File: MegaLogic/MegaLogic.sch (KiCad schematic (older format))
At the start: 17 parts

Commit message: I accidentally solved the Even/Odd problem
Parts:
- added Q? (x4): BC557, Package_TO_SOT_THT:TO-92_Inline, symbol Transistor_BJT:BC557
- added Q? (x4): BC547, Package_TO_SOT_THT:TO-92_Inline, symbol Transistor_BJT:BC547
- added U? (x5): 4070, symbol 4xxx:4070
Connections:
- net Input1: now also U?.1, Q?.2 (B), Q?.2 (B), Q?.2 (B)
- net Input2: now also U?.2, Q?.2 (B), Q?.2 (B)
- net Input3: now also U?.5, Q?.2 (B)
- net Input4: now also U?.6
- net Input5: now also U?.1
- net Input6: now also U?.2
- net Input7: now also U?.5
- net Input8: now also U?.6
- net V+: now also Q?.1 (C), Q?.1 (C), Q?.1 (C), Q?.3 (E)
- net at U?.3: now also U?.9
- net at U?.4: now also U?.8
- net at U?.10: now also U?.13
- net Odd: now reaches U?.11
- net Odd: now also Q?.2 (B)
- net at U?.12: now also U?.10
- new net: Q?.1 (C), Q?.3 (E), Q?.3 (E)
- new net: Q?.3 (E), Q?.3 (E)
- new net: U?.3, U?.9
- new net: U?.4, U?.8
- new net Count1: Q?.1 (C), Q?.3 (E)
- new net Count2: Q?.3 (E)
- new net Even: Q?.1 (C)
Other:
- moved on the sheet: Q?, U?A, U?B, U?C, U?D, U?E

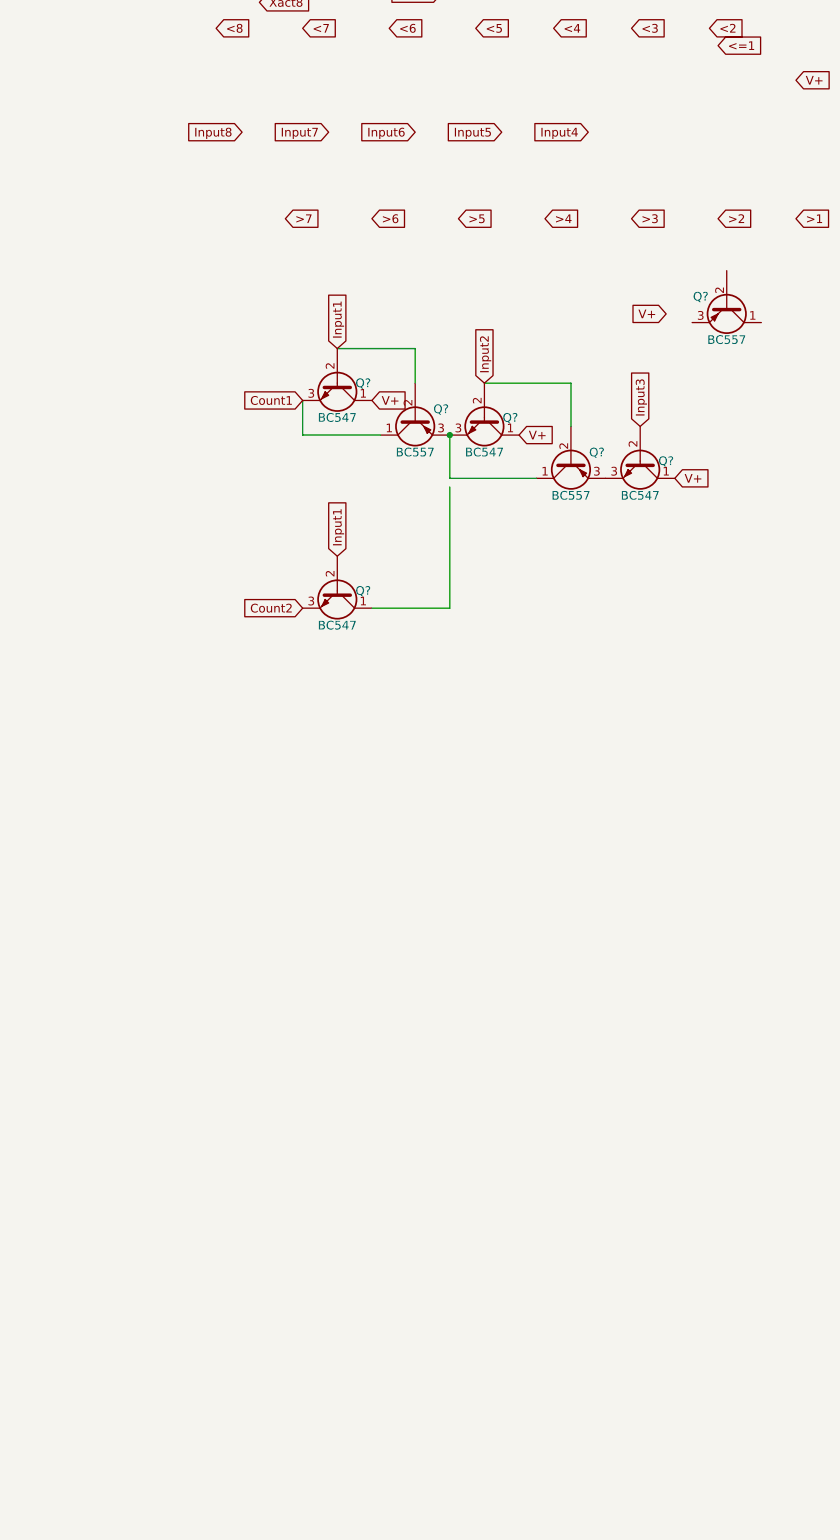
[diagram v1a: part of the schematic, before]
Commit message: I think I solved the Exact count problem
It is the same as the input sorting problem, could be combined?
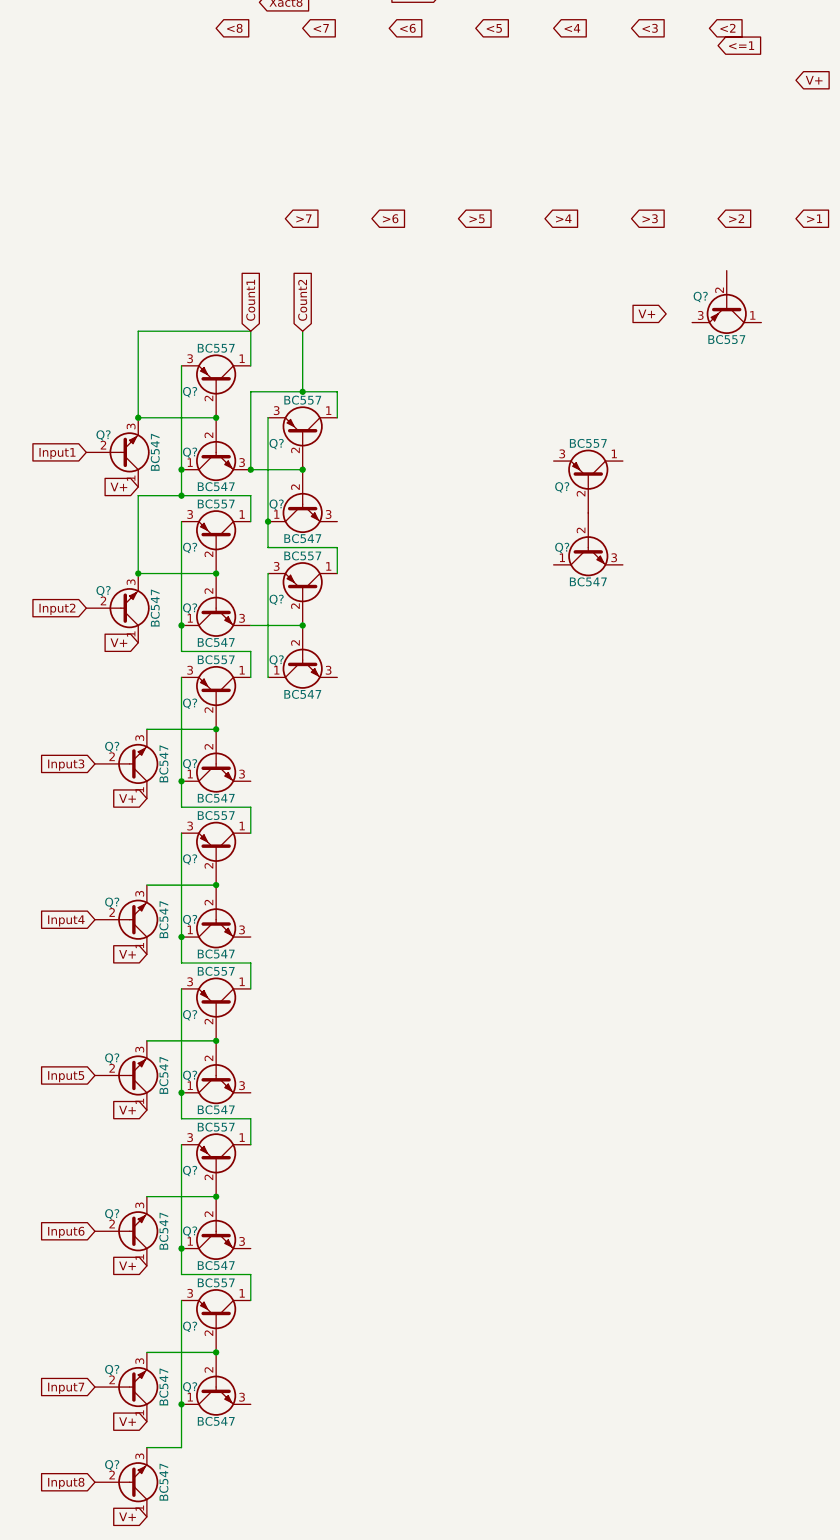
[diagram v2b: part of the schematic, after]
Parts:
- removed Q? (x3): BC547, Package_TO_SOT_THT:TO-92_Inline, symbol Transistor_BJT:BC547
- removed Q?: BC557, Package_TO_SOT_THT:TO-92_Inline, symbol Transistor_BJT:BC557
- added Q? (x17): BC547, Package_TO_SOT_THT:TO-92_Inline, symbol Transistor_BJT:BC547
- added Q? (x9): BC557, Package_TO_SOT_THT:TO-92_Inline, symbol Transistor_BJT:BC557
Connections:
- net Count1: now also Q?.2 (B), Q?.2 (B), Q?.3 (E); no longer Q?.3 (E)
- net Count2: now also Q?.3 (E), Q?.1 (C), Q?.2 (B), Q?.2 (B)
- net Input1: now also Q?.2 (B); no longer Q?.2 (B), Q?.2 (B)
- net Input2: now also Q?.2 (B)
- net Input3: now also Q?.2 (B)
- net Input4: now also Q?.2 (B)
- net Input5: now also Q?.2 (B)
- net Input6: now also Q?.2 (B)
- net Input7: now also Q?.2 (B)
- net Input8: now also Q?.2 (B)
- net V+: now also Q?.1 (C), Q?.1 (C), Q?.1 (C), Q?.1 (C), Q?.1 (C), Q?.1 (C), Q?.1 (C), Q?.1 (C); no longer Q?.1 (C)
- net at Q?.3 (E): now also Q?.1 (C), Q?.1 (C), Q?.2 (B), Q?.2 (B), Q?.3 (E)
- new net: Q?.2 (B), Q?.2 (B), Q?.3 (E) (x6)
- new net: Q?.1 (C), Q?.3 (E), Q?.3 (E)
- new net: Q?.1 (C), Q?.1 (C), Q?.3 (E) (x6)
- new net: Q?.2 (B), Q?.2 (B)
- new net: Q?.1 (C), Q?.3 (E)
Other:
- moved on the sheet: Q?

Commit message: Added Exactly and <> functions
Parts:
- removed Q? (x2): BC557, Package_TO_SOT_THT:TO-92_Inline, symbol Transistor_BJT:BC557
- removed Q?: BC547, Package_TO_SOT_THT:TO-92_Inline, symbol Transistor_BJT:BC547
- added Q? (x48): BC557, Package_TO_SOT_THT:TO-92_Inline, symbol Transistor_BJT:BC557
- added Q? (x55): BC547, Package_TO_SOT_THT:TO-92_Inline, symbol Transistor_BJT:BC547
- added U? (x10): 4069, symbol 4xxx:4070
- added U? (x7): 4069, symbol 4xxx:4069
- U? (x12): value 4070 -> 4069
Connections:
- net <2: now also U?.4
- net <3: now also U?.6
- net <4: now also U?.8
- net <5: now also U?.10
- net <6: now also U?.12
- net <7: now also U?.2
- net <8: now also Q?.1 (C)
- net InputJack1: now also Q?.2 (B)
- net InputJack2: now also Q?.2 (B)
- net InputJack3: now also Q?.2 (B)
- net InputJack4: now also Q?.2 (B)
- net InputJack6: now also Q?.2 (B)
- net InputJack7: now also Q?.2 (B)
- net InputJack8: now also Q?.2 (B)
- net V+: now also Q?.1 (C), Q?.1 (C), Q?.1 (C), Q?.1 (C), Q?.1 (C), Q?.1 (C), Q?.1 (C), Q?.1 (C), Q?.3 (E)
- net Xact1: now also U?.3
- net Xact2: now also U?.4
- net Xact3: now also U?.10
- net Xact4: now also U?.11
- net Xact5: now also U?.3
- net Xact6: now also U?.4
- net Xact7: now also U?.10
- net Xact8: now also Q?.2 (B), Q?.3 (E), U?.9
- net at Q?.2 (B), Q?.2 (B), Q?.3 (E): now also Q?.1 (C), Q?.1 (C), Q?.3 (E)
- net at Q?.3 (E): now also Q?.1 (C), Q?.3 (E), Q?.1 (C), Q?.2 (B), Q?.2 (B)
- net >=3: now reaches Q?.3 (E)
- net >=3: now also Q?.1 (C), Q?.2 (B), Q?.2 (B), U?.5, U?.5, U?.8
- net at Q?.3 (E): now also Q?.1 (C), Q?.1 (C), Q?.2 (B), Q?.2 (B), Q?.3 (E) (x4)
- net at Q?.3 (E): now also Q?.1 (C), Q?.3 (E)
- net Count1 renamed >=1
- net >=1: now also U?.2
- net Count2 renamed >=2
- net >=2: now also U?.1, U?.3, U?.6
- new net: Q?.1 (C), Q?.1 (C), Q?.2 (B), Q?.2 (B), Q?.3 (E), Q?.3 (E) (x25)
- new net: Q?.1 (C), Q?.3 (E), Q?.3 (E) (x12)
- new net: Q?.1 (C), Q?.2 (B), Q?.2 (B), Q?.3 (E) (x7)
- new net: Q?.2 (B), Q?.2 (B), Q?.3 (E) (x5)
- new net: Q?.1 (C), Q?.1 (C), Q?.3 (E) (x5)
- new net >=4: Q?.1 (C), Q?.2 (B), Q?.2 (B), Q?.3 (E), U?.12, U?.9, U?.9
- new net >=5: Q?.1 (C), Q?.2 (B), Q?.2 (B), Q?.3 (E), U?.11, U?.13, U?.2
- new net >=6: Q?.1 (C), Q?.2 (B), Q?.2 (B), Q?.3 (E), U?.1, U?.13, U?.5
- new net >=7: Q?.1 (C), Q?.2 (B), Q?.2 (B), Q?.3 (E), U?.1, U?.6, U?.8
- new net InputJack5: Q?.2 (B)
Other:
- note added: "<2-8"
- note added: "A1"
- note added: "A2"
- note added: "A3"
- note added: "A4"
- note added: "A5"
- note added: "A6"
- note added: "A7"
- note added: "B1"
- note added: "B2"
- note added: "B3"
- note added: "B4"
- note added: "B5"
- note added: "B6"
- note added: "C1"
- note added: "C2"
- note added: "C3"
- note added: "C4"
- note added: "C5"
- note added: "D1"
- note added: "D2"
- note added: "D3"
- note added: "D4"
- note added: "E1"
- note added: "E2"
- note added: "E3"
- note added: "F1"
- note added: "F2"
- note added: "G1"
- note removed: "<=2-8"
- moved on the sheet: Q?

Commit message: Added some new ideas
Problem with 3 voice synth library
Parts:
- added D?: LED, symbol Device:LED
- added D? (x3): D, symbol Device:D
- added J?: AudioJack2_SwitchT, symbol Connector:AudioJack2_SwitchT
- added Q?: BC547, Package_TO_SOT_THT:TO-92_Inline, symbol Transistor_BJT:BC547
- added R?: 15k, symbol Device:R
- added R? (x2): 1.2k, symbol Device:R
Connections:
- net >=1: now also D?.1 (K), Q?.2 (B), R?.2; no longer Q?.2 (B), Q?.2 (B), Q?.3 (E)
- net >=2: now also D?.1 (K); no longer Q?.2 (B), Q?.2 (B), Q?.3 (E)
- net >=3: now also D?.1 (K); no longer Q?.2 (B), Q?.2 (B), Q?.3 (E)
- net GND: now also D?.1 (K), J?.S
- net V+: now also Q?.1 (C)
- new net: D?.2 (A), Q?.2 (B), Q?.2 (B), Q?.3 (E) (x3)
- new net: J?.T, R?.1
- new net: D?.2 (A), R?.1
- new net: Q?.3 (E), R?.1, R?.2, R?.2
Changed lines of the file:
@@
 $EndComp
-Wire Wire Line
-	13000 750  13000 1200
 Wire Wire Line
 	13500 900  13500 750
@@
 Wire Wire Line
 	13000 1200 13300 1200
-Connection ~ 13000 1200
 Connection ~ 13300 1200
 Text Notes 12750 1250 0    50   ~ 10
@@
 	13000 600  13000 450
 Wire Wire Line
-	12350 900  12350 450
-Wire Wire Line
 	12350 450  13000 450
-Connection ~ 12350 900
-Wire Wire Line
-	13500 1500 13500 1050
 Wire Wire Line
 	13500 1050 14000 1050
@@
 Wire Wire Line
 	13500 1500 13800 1500
-Connection ~ 13500 1500
 Connection ~ 13800 1500
 Wire Wire Line
@@
 Connection ~ 15100 2850
 Wire Notes Line
-	11750 400  16350 400
+	11750 -1250 16350 -1250
 Wire Notes Line
 	16350 400  16350 7300
@@
 Connection ~ -2850 3300
 Connection ~ -2750 2850
+$Comp
+L Connector:AudioJack2_SwitchT J?
+U 1 1 5F6FE61C
+P 13200 -750
+F 0 "J?" V 13186 -562 50  0000 L CNN
+F 1 "AudioJack2_SwitchT" V 13277 -562 50  0000 L CNN
+F 2 "" H 13200 -750 50  0001 C CNN
+F 3 "~" H 13200 -750 50  0001 C CNN
+	1    13200 -750
+	0    1    1    0
+$EndComp
+$Comp
+L Device:LED D?
+U 1 1 5F75F938
+P 12750 -700
+F 0 "D?" V 12697 -620 50  0000 L CNN
+F 1 "LED" V 12788 -620 50  0000 L CNN
+F 2 "" H 12750 -700 50  0001 C CNN
+F 3 "~" H 12750 -700 50  0001 C CNN
+	1    12750 -700
+	0    1    1    0
+$EndComp
+$Comp
+L Transistor_BJT:BC547 Q?
+U 1 1 5F7C7DD5
+P 13000 100
+F 0 "Q?" V 12950 250 50  0000 C CNN
+F 1 "BC547" V 13200 100 50  0000 C CNN
+F 2 "Package_TO_SOT_THT:TO-92_Inline" H 13200 25  50  0001 L CIN
+F 3 "http://www.fairchildsemi.com/ds/BC/BC547.pdf" H 13000 100 50  0001 L CNN
+	1    13000 100
+	0    -1   -1   0
+$EndComp
+$Comp
+L Device:R R?
+U 1 1 5F8578AF
+P 13200 150
+F 0 "R?" H 13270 196 50  0000 L CNN
+F 1 "15k" V 13200 50  50  0000 L CNN
+F 2 "" V 13130 150 50  0001 C CNN
+F 3 "~" H 13200 150 50  0001 C CNN
+	1    13200 150
+	1    0    0    -1
+$EndComp
+$Comp
+L Device:R R?
+U 1 1 5F91CAF6
+P 12750 -400
+F 0 "R?" H 12820 -354 50  0000 L CNN
+F 1 "1.2k" V 12750 -500 50  0000 L CNN
+F 2 "" V 12680 -400 50  0001 C CNN
+F 3 "~" H 12750 -400 50  0001 C CNN
+	1    12750 -400
+	1    0    0    -1
+$EndComp
+$Comp
+L Device:R R?
+U 1 1 5F94D7F7
+P 13200 -400
+F 0 "R?" H 13270 -354 50  0000 L CNN
+F 1 "1.2k" V 13200 -500 50  0000 L CNN
+F 2 "" V 13130 -400 50  0001 C CNN
+F 3 "~" H 13200 -400 50  0001 C CNN
+	1    13200 -400
+	1    0    0    -1
+$EndComp
+Wire Wire Line
+	13200 0    13200 -250
+Wire Wire Line
+	13200 -250 12750 -250
+Connection ~ 13200 -250
+Connection ~ 13200 0
+Wire Wire Line
+	13200 300  13000 300
+Wire Wire Line
+	13000 300  13000 450
+Connection ~ 13000 300
+Connection ~ 13000 450
+Text GLabel 12800 0    0    50   Input ~ 0
+V+
+$Comp
+L power:GND #PWR?
+U 1 1 5FB987E7
+P 13300 -550
+F 0 "#PWR?" H 13300 -800 50  0001 C CNN
+F 1 "GND" V 13305 -678 50  0000 R CNN
+F 2 "" H 13300 -550 50  0001 C CNN
+F 3 "" H 13300 -550 50  0001 C CNN
+	1    13300 -550
+	0    -1   -1   0
+$EndComp
+$Comp
+L power:GND #PWR?
+U 1 1 5FB9BF51
+P 12750 -850
+F 0 "#PWR?" H 12750 -1100 50  0001 C CNN
+F 1 "GND" V 12755 -978 50  0000 R CNN
+F 2 "" H 12750 -850 50  0001 C CNN
+F 3 "" H 12750 -850 50  0001 C CNN
+	1    12750 -850
+	-1   0    0    1
+$EndComp
+$Comp
+L Device:D D?
+U 1 1 5FBFD367
+P 12350 600
+F 0 "D?" V 12304 680 50  0000 L CNN
+F 1 "D" V 12395 680 50  0000 L CNN
+F 2 "" H 12350 600 50  0001 C CNN
+F 3 "~" H 12350 600 50  0001 C CNN
+	1    12350 600
+	0    1    1    0
+$EndComp
+Wire Wire Line
+	12350 900  12350 750
+Connection ~ 12350 900
+$Comp
+L Device:D D?
+U 1 1 5FC93CF3
+P 13000 900
+F 0 "D?" V 12954 980 50  0000 L CNN
+F 1 "D" V 13045 980 50  0000 L CNN
+F 2 "" H 13000 900 50  0001 C CNN
+F 3 "~" H 13000 900 50  0001 C CNN
+	1    13000 900
+	0    1    1    0
+$EndComp
+Wire Wire Line
+	13000 1050 13000 1200
+Connection ~ 13000 1200
+$Comp
+L Device:D D?
+U 1 1 5FCF6EE0
+P 13500 1200
+F 0 "D?" V 13454 1280 50  0000 L CNN
+F 1 "D" V 13545 1280 50  0000 L CNN
+F 2 "" H 13500 1200 50  0001 C CNN
+F 3 "~" H 13500 1200 50  0001 C CNN
+	1    13500 1200
+	0    1    1    0
+$EndComp
+Wire Wire Line
+	13500 1350 13500 1500
+Connection ~ 13500 1500
 $EndSCHEMATC
